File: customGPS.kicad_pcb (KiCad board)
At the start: 2 copper layers, 40 x 40 mm, 35 parts, among them J1 C+, J2 C-, J3 U_FL-R-SMT-1_10_, J4 To FC, J6 DRDY, U1 NEO-M8N, U2 LIS3MDL, U3 TLV75733PDBV

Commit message: gerbers
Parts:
- moved C7 109.1 mm to (41.0, 50.5)
- moved FB1 108.3 mm to (37.5, 50.5)
- moved C8 105.9 mm to (45.2, 47.8)
- moved U3 105.9 mm to (45.2, 50.5)
- moved U2 92.4 mm to (34.2, 43.5)
- moved C5 84.7 mm to (33.5, 40.8)
- moved C4 83.2 mm to (31.5, 43.7), turned to -90 degrees
- moved C1 82.6 mm to (27.5, 43.7), turned to -90 degrees
- moved C2 82.1 mm to (29.5, 43.7), turned to -90 degrees
- moved R3 79.8 mm to (38.8, 43.0)
- moved R2 77.5 mm to (38.8, 45.0), turned to 180 degrees
- moved J1 58.6 mm to (51.2, 27.2), turned to 90 degrees
- moved J2 56.1 mm to (51.2, 29.8), turned to 90 degrees
- moved TP2 54.9 mm to (55.0, 37.5)
- moved TP1 54.3 mm to (55.0, 35.0)
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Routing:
- net TimePulse: track 2.27 -> 30.6 mm
- net Net-(U1-~{SAFEBOOT}): track 2.35 -> 30.5 mm
- net GPS_TX: track 0.00 -> 27.8 mm, vias 0 -> 1
- net GPS_RX: track 0.00 -> 27.8 mm, vias 0 -> 1
- net GPS_GND: track 5.66 -> 30.4 mm, vias 3 -> 13
- net GPS_SDA: track 0.00 -> 24.6 mm
- net DRDY: track 0.00 -> 24.5 mm
- net GPS_3.3V: track 6.75 -> 27.9 mm
- net GPS_SCL: track 0.00 -> 20.8 mm
- net GPS_5V: track 0.00 -> 16.8 mm
- net Net-(J3-Pad2): track 2.00 -> 15.7 mm
- net Net-(U3-EN): track 0.00 -> 11.3 mm
- net /GPS_CAP+: track 2.27 -> 8.29 mm
- net Net-(U2-C1): track 0.00 -> 2.41 mm
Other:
- board text added: "Cap Here"
- board text added: "DRDY"

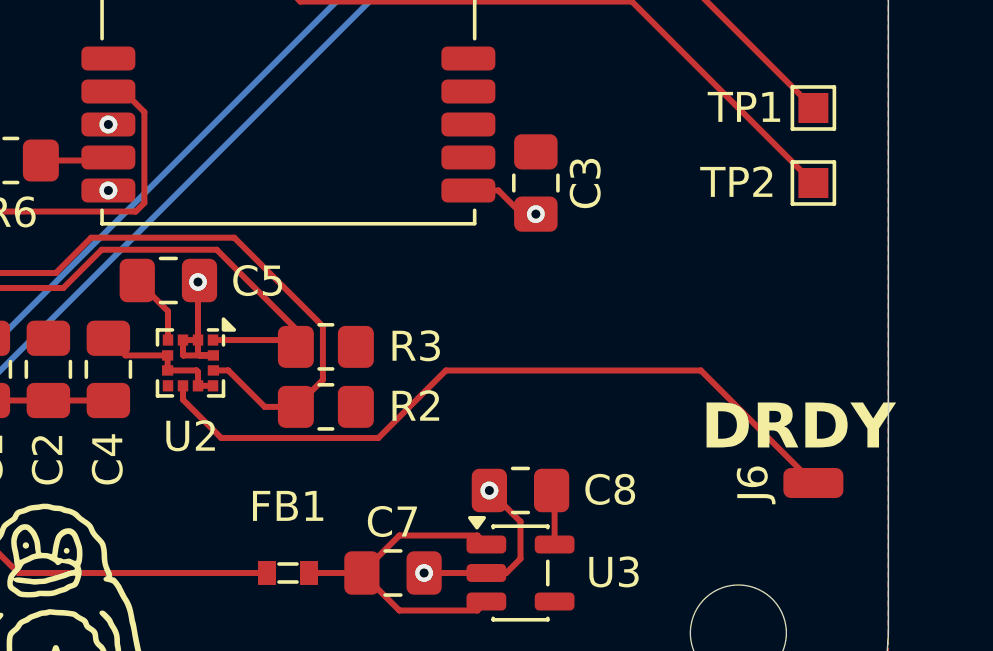
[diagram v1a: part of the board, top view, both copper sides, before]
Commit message: update pcb and fix drc errors
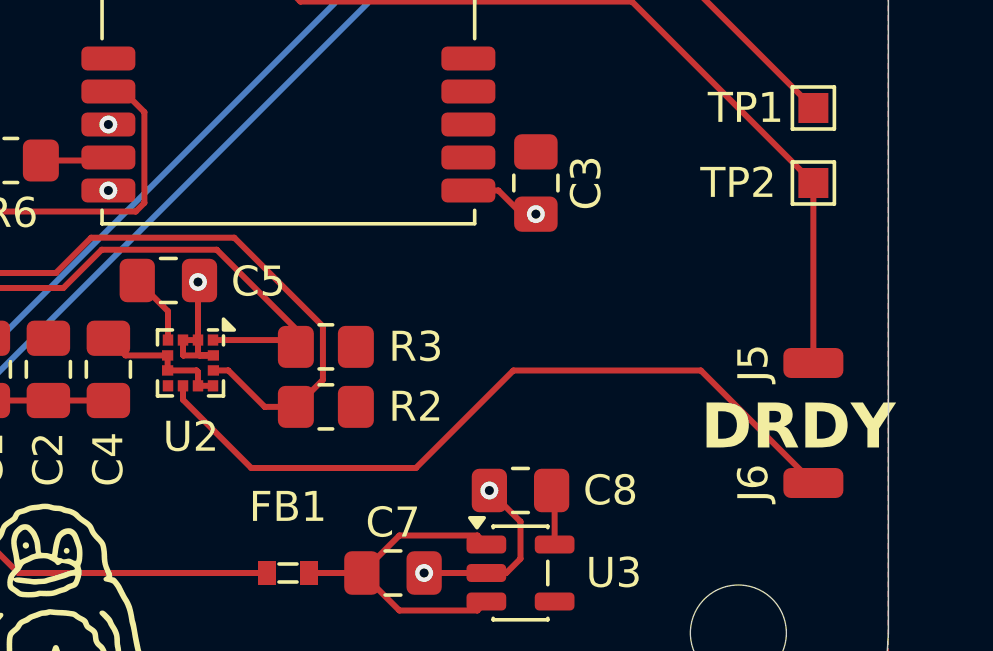
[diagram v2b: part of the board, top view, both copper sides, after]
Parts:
- added J5: TimePulse, Connector_Wire:SolderWirePad_1x01_SMD_1x2mm, F.Cu at (55.0, 43.5)
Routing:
- net TimePulse: track 30.6 -> 36.6 mm
- net DRDY: track 24.5 -> 25.3 mm
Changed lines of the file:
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@@
 		)
 	)
+	(footprint "Connector_Wire:SolderWirePad_1x01_SMD_1x2mm"
+		(layer "F.Cu")
+		(at 55 43.5 90)
+		(descr "Wire Pad, Square, SMD Pad,  1mm x 2mm")
+		(tags "MeasurementPoint Square SMDPad 1mmx2mm ")
+		(property "Reference" "J5"
+			(at 0 -2 90)
+			(layer "F.SilkS")
+			(effects
+				(font
+					(size 1 1)
+					(thickness 0.15)
+				)
+			)
+		)
+		(property "Value" "TimePulse"
+			(at 0 2.54 90)
+			(layer "F.Fab")
+			(effects
+				(font
+					(size 1 1)
+					(thickness 0.15)
+				)
+			)
+		)
+		(property "Datasheet" "~"
+			(at 0 0 90)
+			(unlocked yes)
+			(layer "F.Fab")
+			(hide yes)
+			(effects
+				(font
+					(size 1.27 1.27)
+					(thickness 0.15)
+				)
+			)
+		)
+		(property "Description" "Generic connector, single row, 01x01, script generated (kicad-library-utils/schlib/autogen/connector/)"
+			(at 0 0 90)
+			(unlocked yes)
+			(layer "F.Fab")
+			(hide yes)
+			(effects
+				(font
+					(size 1.27 1.27)
+					(thickness 0.15)
+				)
+			)
+		)
+		(property ki_fp_filters "Connector*:*_1x??_*")
+		(sheetname "/")
+		(sheetfile "customGPS.kicad_sch")
+		(attr exclude_from_pos_files)
+		(fp_rect
+			(start -0.75 -1.25)
+			(end 0.75 1.25)
+			(stroke
+				(width 0.05)
+				(type solid)
+			)
+			(fill no)
+			(layer "F.CrtYd")
+		)
+		(fp_rect
+			(start -0.65 -1.15)
+			(end 0.65 1.15)
+			(stroke
+				(width 0.1)
+				(type solid)
+			)
+			(fill no)
+			(layer "F.Fab")
+		)
+		(fp_text user "${REFERENCE}"
+			(at 0 0 90)
+			(layer "F.Fab")
+			(effects
+				(font
+					(size 1 1)
+					(thickness 0.15)
+				)
+			)
+		)
+		(pad "1" smd roundrect
+			(at 0 0 90)
+			(size 1 2)
+			(layers "F.Cu" "F.Mask")
+			(roundrect_rratio 0.25)
+			(net 5 "TimePulse")
+			(pinfunction "Pin_1")
+			(pintype "passive")
+		)
+		(embedded_fonts no)
+	)
 	(footprint "Capacitor_SMD:C_0805_2012Metric_Pad1.18x1.45mm_HandSolder"
 		(layer "F.Cu")
@@
 	)
 	(segment
+		(start 55 43.5)
+		(end 55 37.5)
+		(width 0.2)
+		(layer "F.Cu")
+		(net 5)
+	)
+	(segment
 		(start 31.45 26)
 		(end 31.5 25.95)
@@
 	)
 	(segment
-		(start 40.5 46)
-		(end 42.75 43.75)
+		(start 33.9875 44.26)
+		(end 33.9875 44.7245)
 		(width 0.2)
 		(layer "F.Cu")
@@
 	)
 	(segment
-		(start 33.9875 44.7245)
-		(end 35.263 46)
+		(start 51.25 43.75)
+		(end 55 47.5)
 		(width 0.2)
 		(layer "F.Cu")
@@
 	)
 	(segment
-		(start 42.75 43.75)
+		(start 45 43.75)
 		(end 51.25 43.75)
 		(width 0.2)
@@
 	)
 	(segment
-		(start 33.9875 44.26)
-		(end 33.9875 44.7245)
+		(start 41.75 47)
+		(end 45 43.75)
 		(width 0.2)
 		(layer "F.Cu")
@@
 	)
 	(segment
-		(start 51.25 43.75)
-		(end 55 47.5)
+		(start 33.9875 44.7245)
+		(end 36.263 47)
 		(width 0.2)
 		(layer "F.Cu")
@@
 	)
 	(segment
-		(start 35.263 46)
-		(end 40.5 46)
+		(start 36.263 47)
+		(end 41.75 47)
 		(width 0.2)
 		(layer "F.Cu")
